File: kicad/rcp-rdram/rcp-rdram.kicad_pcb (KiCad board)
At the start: 2 copper layers, 38.1 x 94 mm, 24 parts, among them P1 RDRAM-EDGE, U11 RDRAM18-NUS, U11-2 RDRAM18-NUS, U14 RDRAM18-NUS, U14-2 RDRAM18-NUS, U15 MX8330, X2 14.705MHz

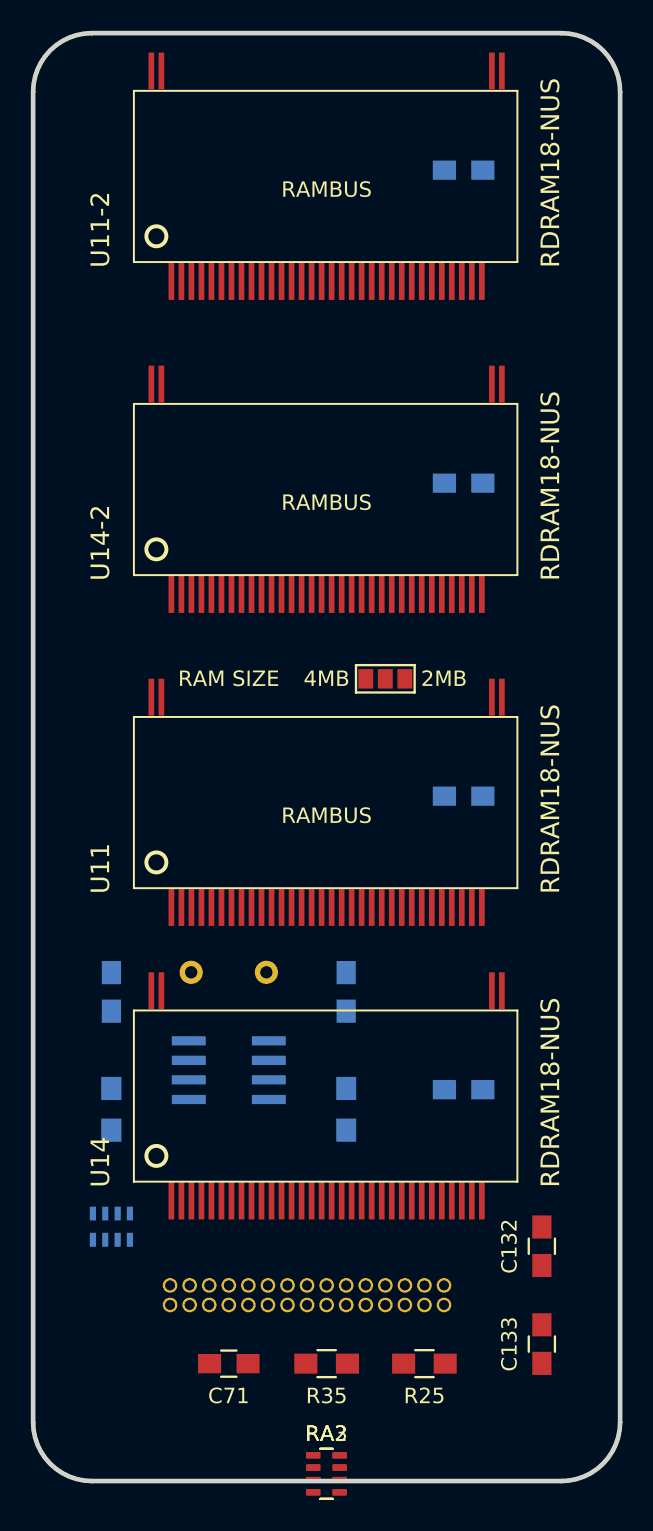
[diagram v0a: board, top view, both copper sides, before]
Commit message: Current layout with 2 mounting holes
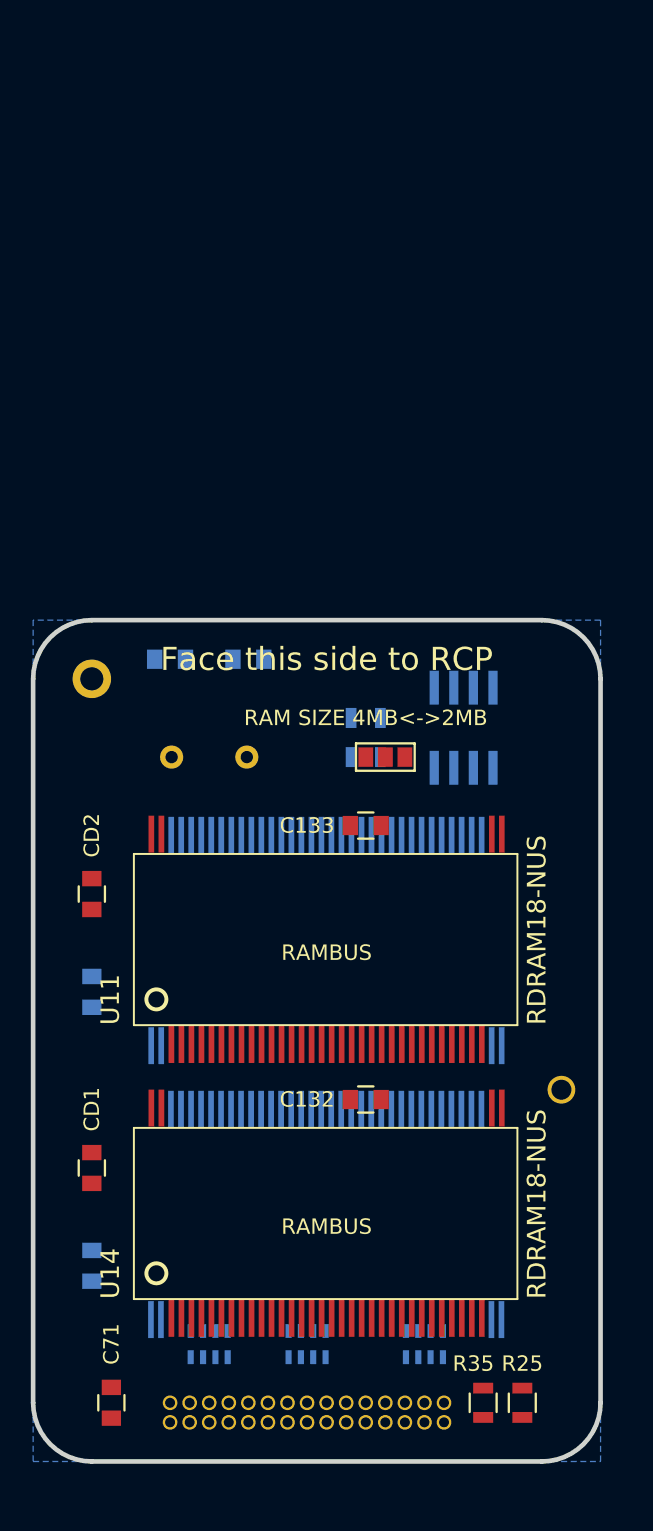
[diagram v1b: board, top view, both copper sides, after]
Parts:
- added REF**: MountingHole_2.2mm_M2_DIN965_Pad, Mounting_Holes:MountingHole_2.2mm_M2_DIN965_Pad, F.Cu at (135.9, 106.7)
- added REF**: MountingHole_2.2mm_M2_DIN965_Pad, Mounting_Holes:MountingHole_2.2mm_M2_DIN965_Pad, F.Cu at (105.4, 80.0)
- C132, C133, C146, C147, C71, CD3, CD4: footprint Capacitors_SMD:C_0805_HandSoldering -> Capacitors_SMD:C_0805
- CD1, CD2: footprint Capacitors_SMD:C_0805_HandSoldering -> Capacitors_SMD:C_0805; moved to F.Cu
- R25, R32, R33, R35: footprint Resistors_SMD:R_0805_HandSoldering -> Resistors_SMD:R_0805
- RA2, RA3, U11-2, U14-2: moved to B.Cu
- U15: value MX8330 -> 8330
- moved CD4 75.1 mm to (105.4, 118.1), turned to 270 degrees
- moved U11-2 65.6 mm to (120.6, 113.9)
- moved CD3 40.9 mm to (105.4, 100.3), turned to 270 degrees
- moved C133 35.5 mm to (123.2, 89.5), turned to 180 degrees
- moved R33 28.2 mm to (123.2, 85.1), turned to 0 degrees
- moved U14-2 27.5 mm to (120.6, 96.1)
- moved U15 26.9 mm to (129.5, 83.2), turned to 180 degrees
- moved R32 25.4 mm to (123.2, 82.5), turned to 180 degrees
- moved CD2 25.0 mm to (105.4, 94.0), turned to 270 degrees
- moved CD1 24.7 mm to (105.4, 111.8), turned to 270 degrees
- moved C147 24.4 mm to (110.5, 78.7), turned to 180 degrees
- moved C146 23.3 mm to (115.6, 78.7), turned to 0 degrees
- moved C132 14.9 mm to (123.2, 107.3), turned to 180 degrees
- moved X2 14.0 mm to (113.0, 85.1), turned to 0 degrees
- moved R35 13.0 mm to (133.3, 127.0), turned to 270 degrees
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- renumbered 4MB to JP1
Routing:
- added copper zone on B.Cu, net GND
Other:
- board size 38.1 x 94 mm -> 36.8 x 54.6 mm
- board text added: "Face this side to RCP"
- board text added: "RAM SIZE 4MB<->2MB"
- board text added: "Top side"
- board text removed: "RAM SIZE"

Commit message: Almost completed, few ratnests are visible yet
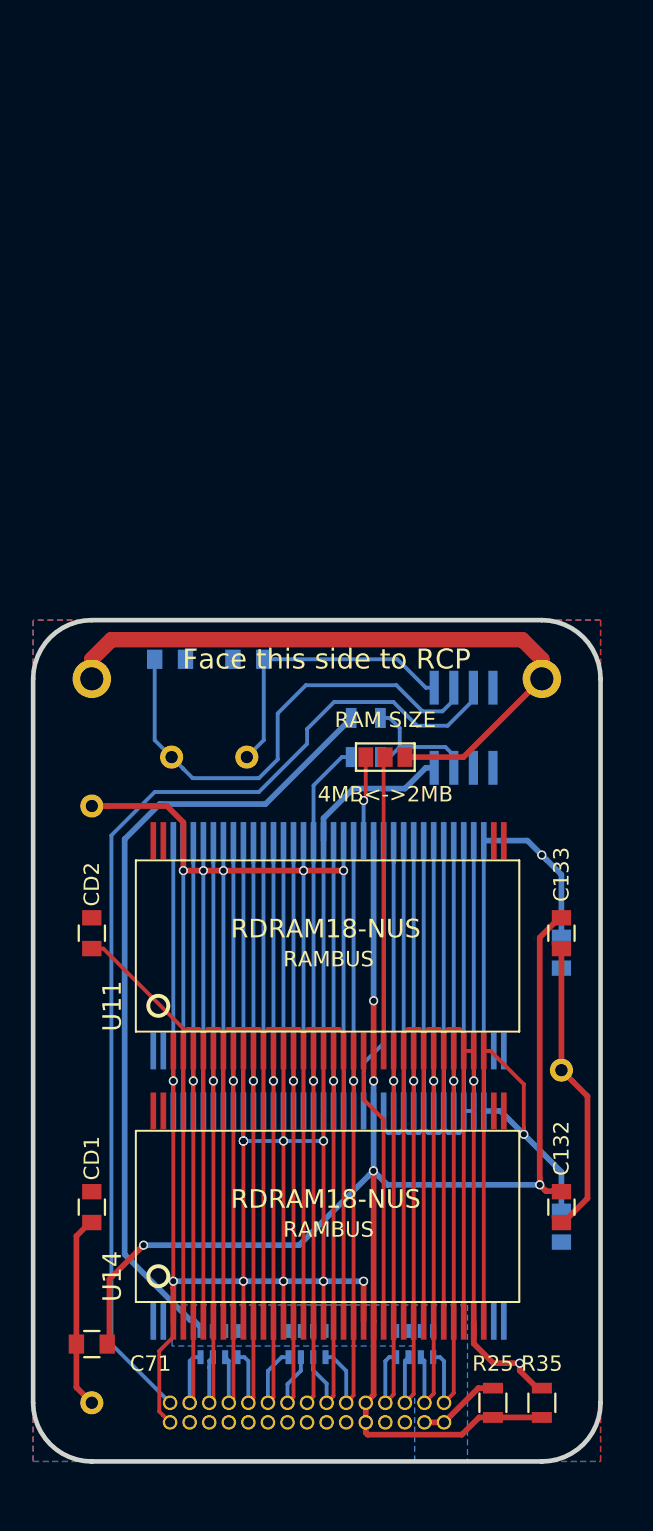
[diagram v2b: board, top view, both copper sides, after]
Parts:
- removed the REF** at (135.9, 106.7)
- added REF**: MountingHole_2.2mm_M2_DIN965_Pad, Mounting_Holes:MountingHole_2.2mm_M2_DIN965_Pad, F.Cu at (134.6, 80.0)
- added REF**: MountingHole_2.2mm_M2_DIN965_Pad, Mounting_Holes:MountingHole_2.2mm_M2_DIN965_Pad, F.Cu at (105.4, 88.3)
- added REF**: MountingHole_2.2mm_M2_DIN965_Pad, Mounting_Holes:MountingHole_2.2mm_M2_DIN965_Pad, F.Cu at (105.4, 127.0)
- added REF**: MountingHole_2.2mm_M2_DIN965_Pad, Mounting_Holes:MountingHole_2.2mm_M2_DIN965_Pad, F.Cu at (135.9, 105.4)
- JP1: value 2MB -> 2/4MB RAM
- U15: value 8330 -> MX8330
- moved CD3 30.6 mm to (135.9, 97.8)
- moved CD4 30.6 mm to (135.9, 115.6)
- moved C132 14.5 mm to (135.9, 114.3), turned to 270 degrees
- moved C133 14.5 mm to (135.9, 96.5), turned to 270 degrees
- moved C146 5.08 mm to (110.5, 78.7)
- moved C147 5.08 mm to (115.6, 78.7)
- moved C71 4.02 mm to (105.4, 123.2), turned to 180 degrees
- moved CD1 2.54 mm to (105.4, 114.3)
- moved CD2 2.54 mm to (105.4, 96.5)
- moved R35 1.27 mm to (134.6, 127.0), turned to 90 degrees
- moved RA1 0.64 mm to (113.7, 123.2)
- moved RA3 0.64 mm to (126.4, 123.2)
- moved R25 0.63 mm to (131.4, 127.0), turned to 270 degrees
- moved U11 0.44 mm to (120.8, 98.2)
- moved U14-2 0.37 mm to (120.8, 96.5)
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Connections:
- U11 pad 26: Net-(U11-Pad26) -> GND
- U11 pad 30: Net-(U11-Pad30) -> GND
- U11 pad 6: Net-(U11-Pad6) -> GND
- U11-2 pad 26: Net-(U11-2-Pad26) -> GND
- U11-2 pad 30: Net-(U11-2-Pad30) -> GND
- U11-2 pad 6: Net-(U11-2-Pad6) -> GND
- U14 pad 26: Net-(U14-Pad26) -> GND
- U14 pad 30: Net-(U14-Pad30) -> GND
- U14 pad 6: Net-(U14-Pad6) -> GND
- U14-2 pad 26: Net-(U14-2-Pad26) -> GND
- U14-2 pad 30: Net-(U14-2-Pad30) -> GND
- U14-2 pad 6: Net-(U14-2-Pad6) -> GND
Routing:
- net GND: track 0.00 -> 539.3 mm, vias 0 -> 7
- net VDD: track 0.00 -> 249.3 mm, vias 0 -> 12
- net /VREF: track 0.00 -> 105.7 mm, vias 0 -> 5
- net Net-(P1-Pad15): track 0.00 -> 68.2 mm
- net /VTERM: track 0.00 -> 57.4 mm
- net /TXCLK: track 0.00 -> 49.4 mm, vias 0 -> 1
- net /COMMAND: track 0.00 -> 46.3 mm, vias 0 -> 1
- net /DQ5: track 0.00 -> 46.3 mm, vias 0 -> 1
- net /DQ0: track 0.00 -> 46.1 mm, vias 0 -> 1
- net /DQ3: track 0.00 -> 46.1 mm, vias 0 -> 1
- net /DQ6: track 0.00 -> 46.0 mm, vias 0 -> 1
- net /DQ8: track 0.00 -> 46.0 mm, vias 0 -> 1
- net /DQ4: track 0.00 -> 45.9 mm, vias 0 -> 1
- net /RXCLK: track 0.00 -> 45.8 mm, vias 0 -> 1
- net /DQ1: track 0.00 -> 45.6 mm, vias 0 -> 1
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- added copper zone on B.Cu, net /VTERM
- added copper zone on F.Cu, net VDD
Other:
- net class Default: clearance 0.2 -> 0.1
- rule trace_clearance: 0.2 -> 0.1

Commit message: Completed, DRC check pass
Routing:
- net GND: track 539.3 -> 556.9 mm, vias 7 -> 8
- net VDD: track 249.3 -> 254.0 mm, vias 12 -> 10
- net Net-(JP1-Pad1): track 5.48 -> 9.38 mm
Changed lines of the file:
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@@
   (general
     (links 199)
-    (no_connects 59)
+    (no_connects 3)
     (area 101.449999 76.049999 138.580001 130.960001)
     (thickness 1.6)
     (drawings 13)
-    (tracks 444)
+    (tracks 475)
     (zones 0)
     (modules 29)
@@
   (segment (start 129.424999 129.070001) (end 130.545 127.95) (width 0.37) (layer F.Cu) (net 1))
   (segment (start 130.545 127.95) (end 131.445 127.95) (width 0.37) (layer F.Cu) (net 1))
+  (segment (start 113.949999 108.059999) (end 113.949999 109.200001) (width 0.25) (layer B.Cu) (net 2))
+  (segment (start 113.949999 109.200001) (end 114.234998 109.485) (width 0.25) (layer B.Cu) (net 2))
+  (segment (start 114.234998 109.485) (end 116.265 109.485) (width 0.25) (layer B.Cu) (net 2))
+  (segment (start 116.265 109.485) (end 116.549999 109.200001) (width 0.25) (layer B.Cu) (net 2))
+  (segment (start 116.549999 109.200001) (end 116.549999 108.059999) (width 0.25) (layer B.Cu) (net 2))
+  (segment (start 113.949999 109.200001) (end 113.665 109.485) (width 0.25) (layer B.Cu) (net 2))
+  (segment (start 113.665 109.485) (end 112.934998 109.485) (width 0.25) (layer B.Cu) (net 2))
+  (segment (start 112.934998 109.485) (end 112.649999 109.200001) (width 0.25) (layer B.Cu) (net 2))
+  (segment (start 112.649999 109.200001) (end 112.649999 108.059999) (width 0.25) (layer B.Cu) (net 2))
+  (segment (start 129.55 90.51) (end 130.2 90.51) (width 0.25) (layer B.Cu) (net 2))
+  (segment (start 128.25 90.51) (end 128.25 89.369998) (width 0.25) (layer B.Cu) (net 2))
+  (segment (start 128.25 89.369998) (end 128.534999 89.084999) (width 0.25) (layer B.Cu) (net 2))
+  (segment (start 128.534999 89.084999) (end 129.265001 89.084999) (width 0.25) (layer B.Cu) (net 2))
+  (segment (start 129.265001 89.084999) (end 129.55 89.369998) (width 0.25) (layer B.Cu) (net 2))
+  (segment (start 129.55 89.369998) (end 129.55 90.51) (width 0.25) (layer B.Cu) (net 2))
+  (segment (start 126.95 90.51) (end 126.95 89.369998) (width 0.25) (layer B.Cu) (net 2))
+  (segment (start 126.95 89.369998) (end 127.234999 89.084999) (width 0.25) (layer B.Cu) (net 2))
+  (segment (start 127.234999 89.084999) (end 127.965001 89.084999) (width 0.25) (layer B.Cu) (net 2))
+  (segment (start 127.965001 89.084999) (end 128.25 89.369998) (width 0.25) (layer B.Cu) (net 2))
+  (segment (start 125.65 90.51) (end 125.65 89.369998) (width 0.25) (layer B.Cu) (net 2))
+  (segment (start 125.65 89.369998) (end 125.934999 89.084999) (width 0.25) (layer B.Cu) (net 2))
+  (segment (start 125.934999 89.084999) (end 126.665001 89.084999) (width 0.25) (layer B.Cu) (net 2))
+  (segment (start 126.665001 89.084999) (end 126.95 89.369998) (width 0.25) (layer B.Cu) (net 2))
+  (segment (start 116.549999 92.46) (end 116.549999 108.059999) (width 0.25) (layer B.Cu) (net 2))
+  (segment (start 116.549999 90.51) (end 116.549999 92.46) (width 0.25) (layer B.Cu) (net 2))
+  (via (at 116.549999 92.46) (size 0.6) (drill 0.4) (layers F.Cu B.Cu) (net 2))
   (segment (start 121.75 92.46) (end 119.149999 92.46) (width 0.37) (layer F.Cu) (net 2))
   (segment (start 121.75 92.46) (end 121.75 108.059999) (width 0.25) (layer B.Cu) (net 2))
@@
   (segment (start 104.41 123.19) (end 104.41 126) (width 0.37) (layer F.Cu) (net 2))
   (segment (start 104.41 126) (end 105.41 127) (width 0.37) (layer F.Cu) (net 2))
-  (segment (start 116.549999 90.51) (end 116.549999 108.059999) (width 0.25) (layer B.Cu) (net 2))
   (segment (start 125.65 108.059999) (end 125.65 90.51) (width 0.25) (layer B.Cu) (net 2))
   (segment (start 126.95 108.059999) (end 126.95 90.51) (width 0.25) (layer B.Cu) (net 2))
@@
   (segment (start 116.57 78.74) (end 116.57 83.99094) (width 0.25) (layer B.Cu) (net 4))
   (segment (start 116.57 83.99094) (end 115.47094 85.09) (width 0.25) (layer B.Cu) (net 4))
-  (segment (start 115.25 110.01) (end 117.85 110.01) (width 0.25) (layer B.Cu) (net 5))
-  (segment (start 117.85 110.01) (end 120.449999 110.01) (width 0.25) (layer B.Cu) (net 5))
+  (segment (start 130.85 90.51) (end 130.85 89.06) (width 0.37) (layer B.Cu) (net 5))
+  (segment (start 128.622969 88.353831) (end 127.635062 87.365924) (width 0.37) (layer B.Cu) (net 5))
+  (segment (start 130.143831 88.353831) (end 128.622969 88.353831) (width 0.37) (layer B.Cu) (net 5))
+  (segment (start 130.85 89.06) (end 130.143831 88.353831) (width 0.37) (layer B.Cu) (net 5))
+  (segment (start 127.635062 87.365924) (end 127.635062 85.785063) (width 0.37) (layer B.Cu) (net 5))
+  (segment (start 120.449999 90.51) (end 120.449999 88.360947) (width 0.37) (layer B.Cu) (net 5))
+  (segment (start 120.449999 88.360947) (end 122.181988 86.628958) (width 0.37) (layer B.Cu) (net 5))
+  (segment (start 127.085062 85.785063) (end 127.635062 85.785063) (width 0.37) (layer B.Cu) (net 5))
+  (segment (start 122.181988 86.628958) (end 126.241167 86.628958) (width 0.37) (layer B.Cu) (net 5))
+  (segment (start 126.241167 86.628958) (end 127.085062 85.785063) (width 0.37) (layer B.Cu) (net 5))
+  (segment (start 120.449999 110.01) (end 117.85 110.01) (width 0.25) (layer B.Cu) (net 5))
+  (segment (start 120.449999 119.11) (end 123.05 119.11) (width 0.37) (layer B.Cu) (net 5))
+  (segment (start 117.849999 119.11) (end 120.449999 119.11) (width 0.37) (layer B.Cu) (net 5))
+  (segment (start 115.249999 119.11) (end 117.849999 119.11) (width 0.37) (layer B.Cu) (net 5))
+  (segment (start 110.7 119.11) (end 115.249999 119.11) (width 0.37) (layer B.Cu) (net 5))
+  (segment (start 115.249999 90.51) (end 115.249999 89.369998) (width 0.25) (layer B.Cu) (net 5))
+  (segment (start 115.249999 89.369998) (end 115.534998 89.084999) (width 0.25) (layer B.Cu) (net 5))
+  (segment (start 115.534998 89.084999) (end 117.565 89.084999) (width 0.25) (layer B.Cu) (net 5))
+  (segment (start 117.565 89.084999) (end 117.849999 89.369998) (width 0.25) (layer B.Cu) (net 5))
+  (segment (start 117.849999 89.369998) (end 117.849999 90.51) (width 0.25) (layer B.Cu) (net 5))
   (segment (start 117.849999 108.059999) (end 117.849999 110.009999) (width 0.25) (layer B.Cu) (net 5))
   (segment (start 117.849999 110.009999) (end 117.85 110.01) (width 0.25) (layer B.Cu) (net 5))
   (via (at 117.85 110.01) (size 0.6) (drill 0.4) (layers F.Cu B.Cu) (net 5))
-  (via (at 115.25 110.01) (size 0.6) (drill 0.4) (layers F.Cu B.Cu) (net 5))
-  (segment (start 115.249999 108.059999) (end 115.249999 110.009999) (width 0.25) (layer B.Cu) (net 5))
-  (segment (start 115.249999 110.009999) (end 115.25 110.01) (width 0.25) (layer B.Cu) (net 5))
-  (via (at 115.25 110.01) (size 0.6) (drill 0.4) (layers F.Cu B.Cu) (net 5))
   (segment (start 120.449999 108.059999) (end 120.449999 110.01) (width 0.25) (layer B.Cu) (net 5))
   (segment (start 120.449999 108.06) (end 120.449999 104.16) (width 0.25) (layer F.Cu) (net 5))
@@
   (segment (start 120.449999 108.06) (end 120.449999 110.01) (width 0.25) (layer F.Cu) (net 5))
   (via (at 120.449999 110.01) (size 0.6) (drill 0.4) (layers F.Cu B.Cu) (net 5))
-  (segment (start 123.05 119.11) (end 110.7 119.11) (width 0.37) (layer B.Cu) (net 5))
   (segment (start 120.449999 90.51) (end 120.449999 108.059999) (width 0.25) (layer B.Cu) (net 5))
   (segment (start 130.85 104.16) (end 131.285 104.16) (width 0.25) (layer F.Cu) (net 5))
@@
   (segment (start 133.45 106.325) (end 133.45 109.150076) (width 0.25) (layer F.Cu) (net 5))
   (segment (start 133.45 109.150076) (end 133.45 109.57434) (width 0.25) (layer F.Cu) (net 5))
-  (segment (start 133.45 109.57434) (end 131.935659 108.059999) (width 0.37) (layer B.Cu) (net 5))
   (segment (start 135.89 112.01434) (end 133.45 109.57434) (width 0.37) (layer B.Cu) (net 5))
   (via (at 133.45 109.57434) (size 0.6) (drill 0.4) (layers F.Cu B.Cu) (net 5))
@@
   (via (at 110.699999 106.11) (size 0.6) (drill 0.4) (layers F.Cu B.Cu) (net 5))
   (segment (start 135.89 114.57) (end 135.89 112.01434) (width 0.37) (layer B.Cu) (net 5))
-  (segment (start 131.935659 108.059999) (end 130.85 108.059999) (width 0.37) (layer B.Cu) (net 5))
-  (segment (start 120.449999 90.51) (end 120.449999 89.06) (width 0.37) (layer B.Cu) (net 5))
-  (segment (start 127.085062 85.785063) (end 127.635062 85.785063) (width 0.37) (layer B.Cu) (net 5))
-  (segment (start 125.735062 87.135063) (end 127.085062 85.785063) (width 0.37) (layer B.Cu) (net 5))
-  (segment (start 122.374936 87.135063) (end 125.735062 87.135063) (width 0.37) (layer B.Cu) (net 5))
-  (segment (start 120.449999 89.06) (end 122.374936 87.135063) (width 0.37) (layer B.Cu) (net 5))
   (segment (start 134.615788 91.44606) (end 133.679728 90.51) (width 0.37) (layer B.Cu) (net 5))
   (via (at 134.615788 91.44606) (size 0.6) (drill 0.4) (layers F.Cu B.Cu) (net 5))
@@
   (segment (start 124.35 103.65915) (end 124.35 90.51) (width 0.25) (layer B.Cu) (net 24))
   (segment (start 123.05 108.059999) (end 123.05 104.95915) (width 0.25) (layer B.Cu) (net 24))
-  (segment (start 123.19 87.77) (end 123.05 87.91) (width 0.25) (layer F.Cu) (net 27))
-  (segment (start 123.19 85.09) (end 123.19 87.77) (width 0.25) (layer F.Cu) (net 27))
-  (segment (start 123.05 87.91) (end 123.05 90.51) (width 0.25) (layer B.Cu) (net 27))
-  (via (at 123.05 87.91) (size 0.6) (drill 0.4) (layers F.Cu B.Cu) (net 27))
+  (segment (start 123.05 92.46) (end 123.05 90.51) (width 0.25) (layer B.Cu) (net 27))
+  (segment (start 123.19 85.09) (end 123.19 92.32) (width 0.25) (layer F.Cu) (net 27))
+  (segment (start 123.19 92.32) (end 123.05 92.46) (width 0.25) (layer F.Cu) (net 27))
+  (via (at 123.05 92.46) (size 0.6) (drill 0.4) (layers F.Cu B.Cu) (net 27))
   (zone (net 2) (net_name GND) (layer B.Cu) (hatch edge 0.508)
     (connect_pads (clearance 0.508))
